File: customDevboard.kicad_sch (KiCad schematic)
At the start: 44 parts, among them J2 USB_C_Receptacle_USB2.0_14P, J20 From BEC, J6 Debug, J7 To GPS, J8 BZ+, J9 COL, Q1 BC817, Q2 AO3401A, U3 TPD2EUSB30, U5 STM32F722RET6, U6 TLV75733PDRV, Y1 8MHz, Y2 32.768KHz

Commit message: ready for production almost
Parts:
- added J1, J10, J11, J12, J13, J14, J15, J16, J17, J18, J19, J21, J22, J23, J24, J25, J26, J27, J3, J4, J5: Conn_01x01, Connector_Wire:SolderWirePad_1x01_SMD_1x2mm, symbol Connector_Generic:Conn_01x01
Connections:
- net PC3: now reaches U5.11 (PC3)
- net PC3: now also J24.1 (Pin_1)
- net PA0: now reaches U5.14 (PA0)
- net PA0: now also J25.1 (Pin_1)
- net PA1: now reaches U5.15 (PA1)
- net PA1: now also J26.1 (Pin_1)
- net PB2: now reaches U5.27 (PB2)
- net PB2: now also J27.1 (Pin_1)
- net PB12: now reaches U5.33 (PB12)
- net PB12: now also J22.1 (Pin_1)
- net PB14: now reaches U5.35 (PB14)
- net PB14: now also J21.1 (Pin_1)
- net PB15: now reaches U5.36 (PB15)
- net PB15: now also J19.1 (Pin_1)
- net PC6: now reaches U5.37 (PC6)
- net PC6: now also J18.1 (Pin_1)
- net PC7: now reaches U5.38 (PC7)
- net PC7: now also J17.1 (Pin_1)
- net PC8: now reaches U5.39 (PC8)
- net PC8: now also J16.1 (Pin_1)
- net PC9: now reaches U5.40 (PC9)
- net PC9: now also J15.1 (Pin_1)
- net PA8: now reaches U5.41 (PA8)
- net PA8: now also J14.1 (Pin_1)
- net PA15: now reaches U5.50 (PA15)
- net PA15: now also J13.1 (Pin_1)
- net PC12: now reaches U5.53 (PC12)
- net PC12: now also J12.1 (Pin_1)
- net PD2: now reaches U5.54 (PD2)
- net PD2: now also J11.1 (Pin_1)
- net PB3: now reaches U5.55 (PB3)
- net PB3: now also J10.1 (Pin_1)
- net PB4: now reaches U5.56 (PB4)
- net PB4: now also J5.1 (Pin_1)
- net PB5: now reaches U5.57 (PB5)
- net PB5: now also J4.1 (Pin_1)
- net PB8: now reaches U5.61 (PB8)
- net PB8: now also J3.1 (Pin_1)
- net PB9: now reaches U5.62 (PB9)
- net PB9: now also J1.1 (Pin_1)
- net PC0: now reaches U5.8 (PC0)
- net PC0: now also J23.1 (Pin_1)
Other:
- removed sheet ESC
- note added: "Breakout pads"
- moved on the sheet: C24, C25, C26, D1, FB1, J6, R19, TP5, Y1, Y2

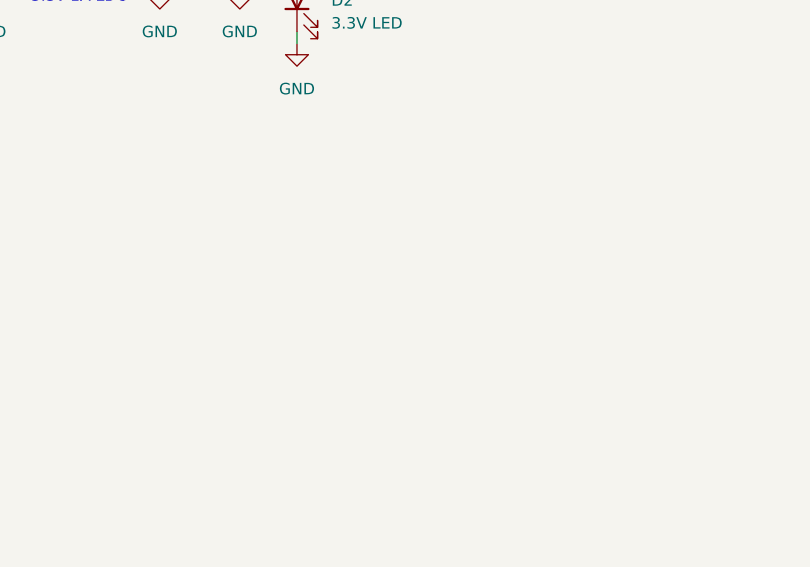
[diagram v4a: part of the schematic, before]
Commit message: fix drc issues and blender render
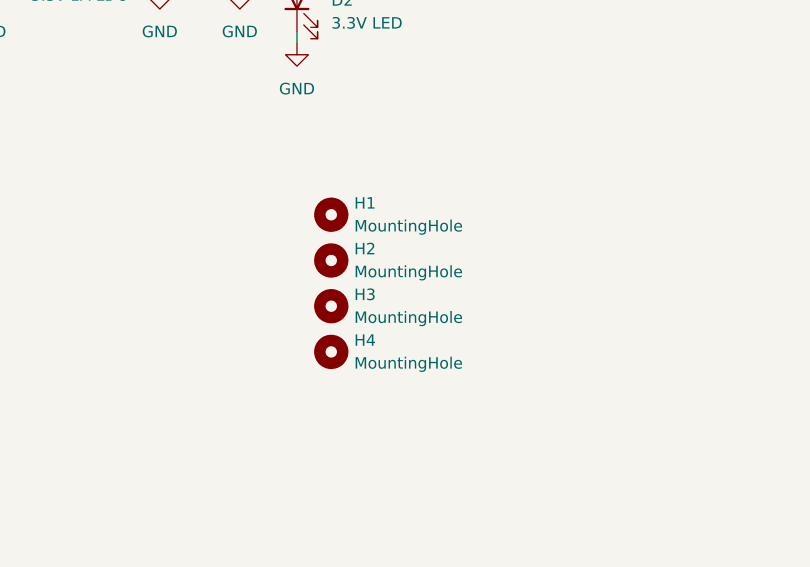
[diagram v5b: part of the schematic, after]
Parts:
- added H1, H2, H3, H4: MountingHole, MountingHole:MountingHole_3.2mm_M3, symbol Mechanical:MountingHole

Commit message: firmware and readme
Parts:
- added J28: PA6, Connector_Wire:SolderWirePad_1x01_SMD_1x2mm, symbol Connector_Generic:Conn_01x01
- added J29: PA5, Connector_Wire:SolderWirePad_1x01_SMD_1x2mm, symbol Connector_Generic:Conn_01x01
- added J30: PC1, Connector_Wire:SolderWirePad_1x01_SMD_1x2mm, symbol Connector_Generic:Conn_01x01
- added J31, J35: PC11, Connector_Wire:SolderWirePad_1x01_SMD_1x2mm, symbol Connector_Generic:Conn_01x01
- added J32: PB13, Connector_Wire:SolderWirePad_1x01_SMD_1x2mm, symbol Connector_Generic:Conn_01x01
- added J33: PA4, Connector_Wire:SolderWirePad_1x01_SMD_1x2mm, symbol Connector_Generic:Conn_01x01
- added J34: PB2, Connector_Wire:SolderWirePad_1x01_SMD_1x2mm, symbol Connector_Generic:Conn_01x01
- added J36: PC10, Connector_Wire:SolderWirePad_1x01_SMD_1x2mm, symbol Connector_Generic:Conn_01x01
- added J37: PB6, Connector_Wire:SolderWirePad_1x01_SMD_1x2mm, symbol Connector_Generic:Conn_01x01
- added J38: PB7, Connector_Wire:SolderWirePad_1x01_SMD_1x2mm, symbol Connector_Generic:Conn_01x01
- added J39: PA9, Connector_Wire:SolderWirePad_1x01_SMD_1x2mm, symbol Connector_Generic:Conn_01x01
- added J40: PA10, Connector_Wire:SolderWirePad_1x01_SMD_1x2mm, symbol Connector_Generic:Conn_01x01
- added J41: PA2, Connector_Wire:SolderWirePad_1x01_SMD_1x2mm, symbol Connector_Generic:Conn_01x01
- added J42: PA3, Connector_Wire:SolderWirePad_1x01_SMD_1x2mm, symbol Connector_Generic:Conn_01x01
- added J43: PB10, Connector_Wire:SolderWirePad_1x01_SMD_1x2mm, symbol Connector_Generic:Conn_01x01
- added J44: PB11, Connector_Wire:SolderWirePad_1x01_SMD_1x2mm, symbol Connector_Generic:Conn_01x01
- J25: value Conn_01x01 -> PA0
- J26: value Conn_01x01 -> PA1
- J27: value Conn_01x01 -> PA7
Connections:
- net I2C1_SCL: now also J37.1 (Pin_1)
- net I2C1_SDA: now also J38.1 (Pin_1)
- net SPI1_MISO: now also J28.1 (Pin_1)
- net SPI1_MOSI: now also J27.1 (Pin_1)
- net SPI1_SCK: now also J29.1 (Pin_1)
- net SPI2_MISO: now also J31.1 (Pin_1)
- net SPI2_MOSI: now also J30.1 (Pin_1)
- net SPI2_SCK: now also J32.1 (Pin_1)
- net SPI3_MISO: now also J35.1 (Pin_1)
- net SPI3_NSS: now also J33.1 (Pin_1)
- net SPI3_SCK: now also J36.1 (Pin_1)
- net USART1_RX: now also J40.1 (Pin_1)
- net USART1_TX: now also J39.1 (Pin_1)
- net USART2_RX: now also J42.1 (Pin_1)
- net USART2_TX: now also J41.1 (Pin_1)
- net USART3_RX: now also J44.1 (Pin_1)
- net USART3_TX: now also J43.1 (Pin_1)
- net PB2 renamed SPI3_MOSI
- net SPI3_MOSI: now also J34.1 (Pin_1); no longer J27.1 (Pin_1)
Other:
- note added: "For IMU"
- note added: "to GPS and barometer"
- moved on the sheet: H1, H2, H3, H4

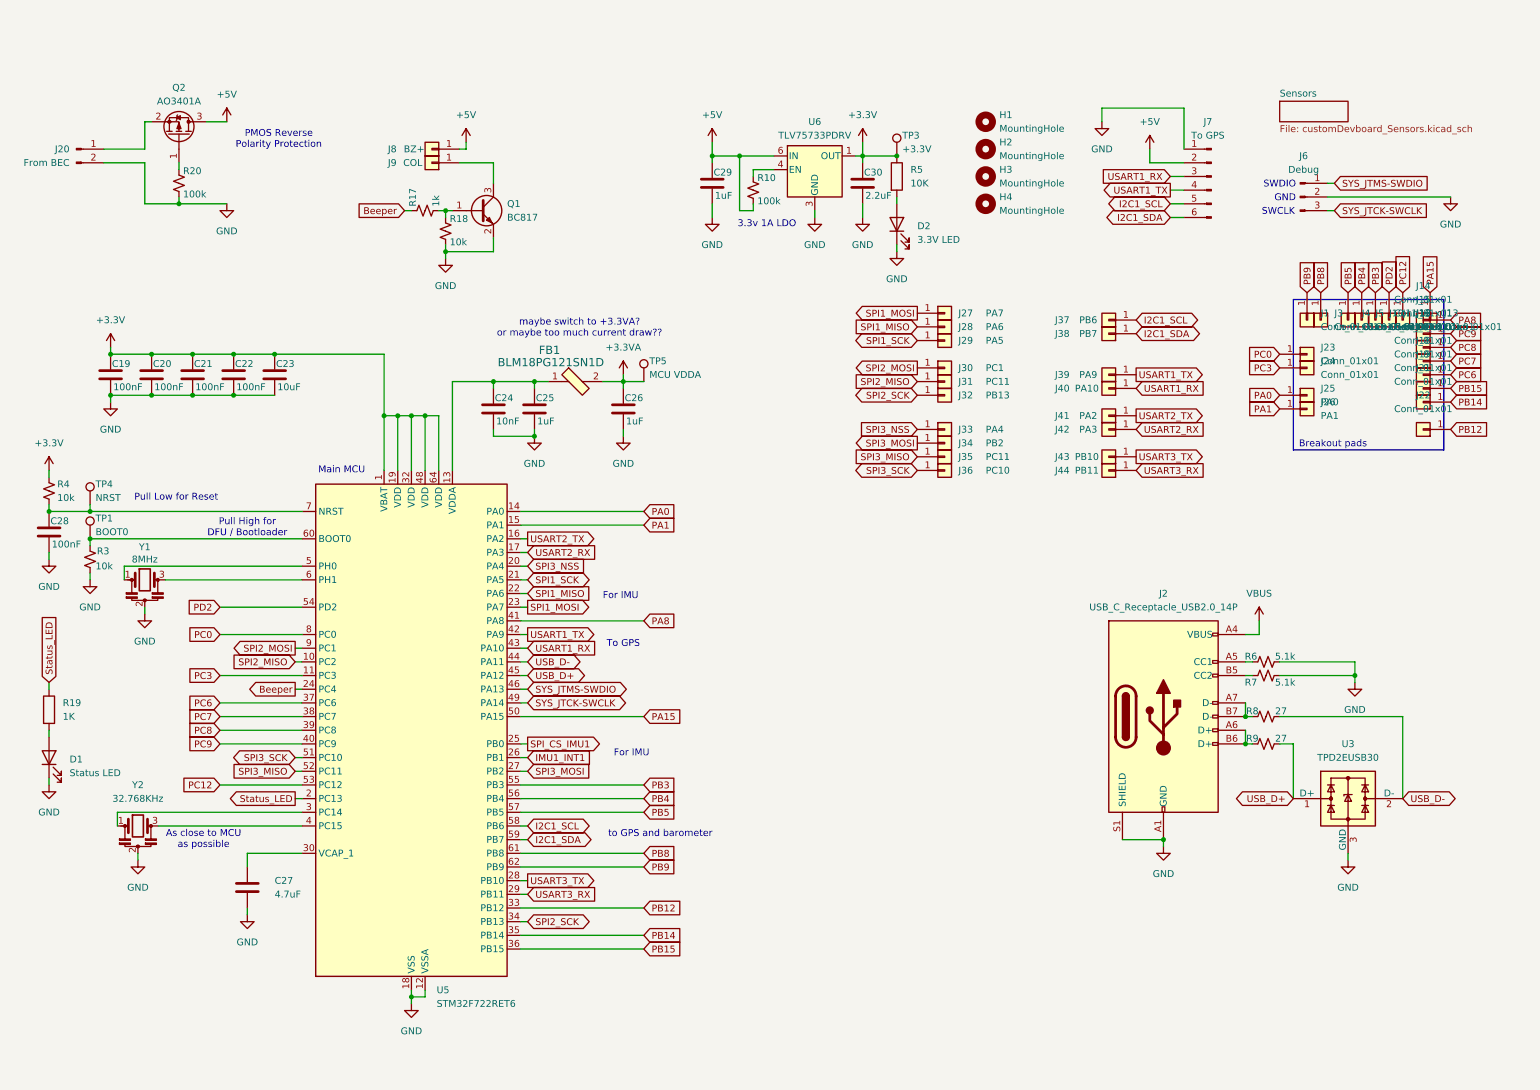
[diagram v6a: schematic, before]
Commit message: add switches and fix drc
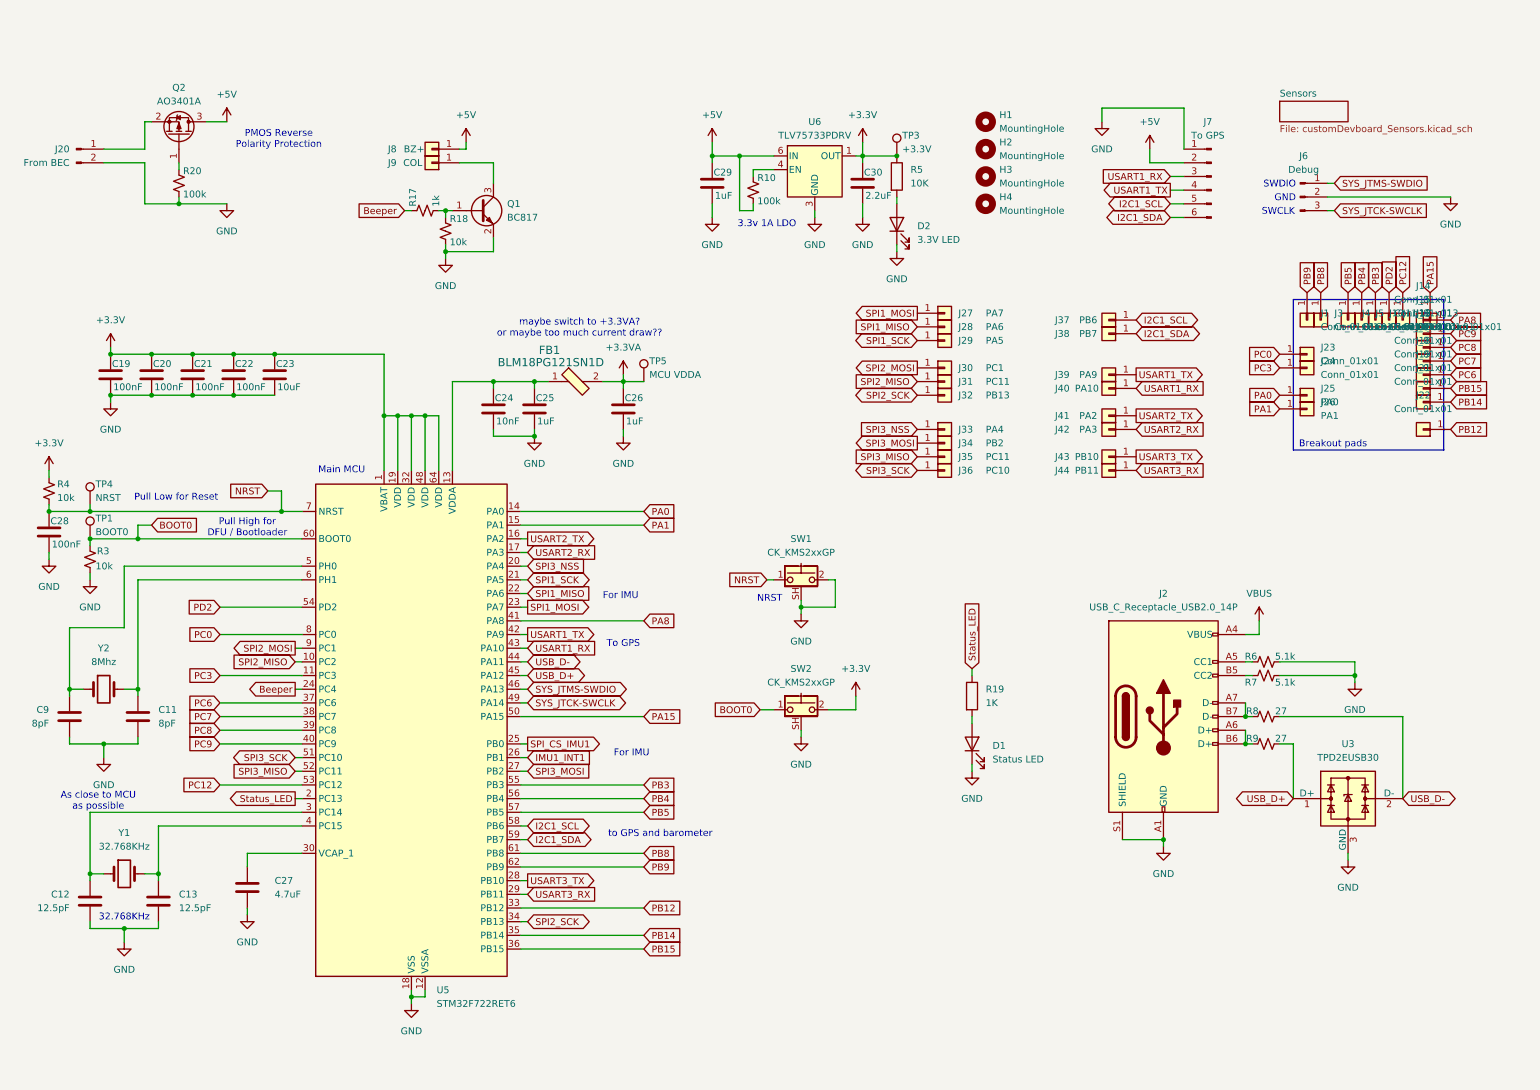
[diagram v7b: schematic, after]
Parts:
- removed Y1: 8MHz, Crystal:Resonator_SMD_Murata_CSTxExxV-3Pin_3.0x1.1mm, symbol Device:Resonator
- removed Y2: 32.768KHz, Crystal:Resonator_SMD_Murata_CSTxExxV-3Pin_3.0x1.1mm, symbol Device:Resonator
- added C11, C9: 8pF, Capacitor_SMD:C_0603_1608Metric, symbol Device:C
- added C12, C13: 12.5pF, Capacitor_SMD:C_0603_1608Metric, symbol Device:C
- added SW1, SW2: CK_KMS2xxGP, Button_Switch_SMD:SW_SPST_CK_KMS2xxGP, symbol Switch:CK_KMS2xxGP
- added Y1: 32.768KHz, Crystal:Crystal_SMD_2012-2Pin_2.0x1.2mm, symbol Device:Crystal
- added Y2: 8Mhz, Crystal:Crystal_SMD_2012-2Pin_2.0x1.2mm, symbol Device:Crystal
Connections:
- net +3.3V: now also SW2.2
- net GND: now also C11.2, C12.2, C13.2, C9.2, SW1.2, SW1.SH (B), SW2.SH (B)
- net NRST: now reaches C28.1, R4.2, TP4.1, U5.7 (NRST)
- net NRST: now also SW1.1
- net at U5.3 (PC14): now also C12.1, Y1.1
- net at U5.4 (PC15): now also C13.1, Y1.2
- net at U5.5 (PH0): now also C9.1, Y2.1
- net at U5.6 (PH1): now also C11.1, Y2.2
- net BOOT0: now reaches R3.1, TP1.1, U5.60 (BOOT0)
- net BOOT0: now also SW2.1
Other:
- note added: "32.768KHz"
- note added: "NRST"
- moved on the sheet: D1, R19

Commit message: restart pcb because too many new parts
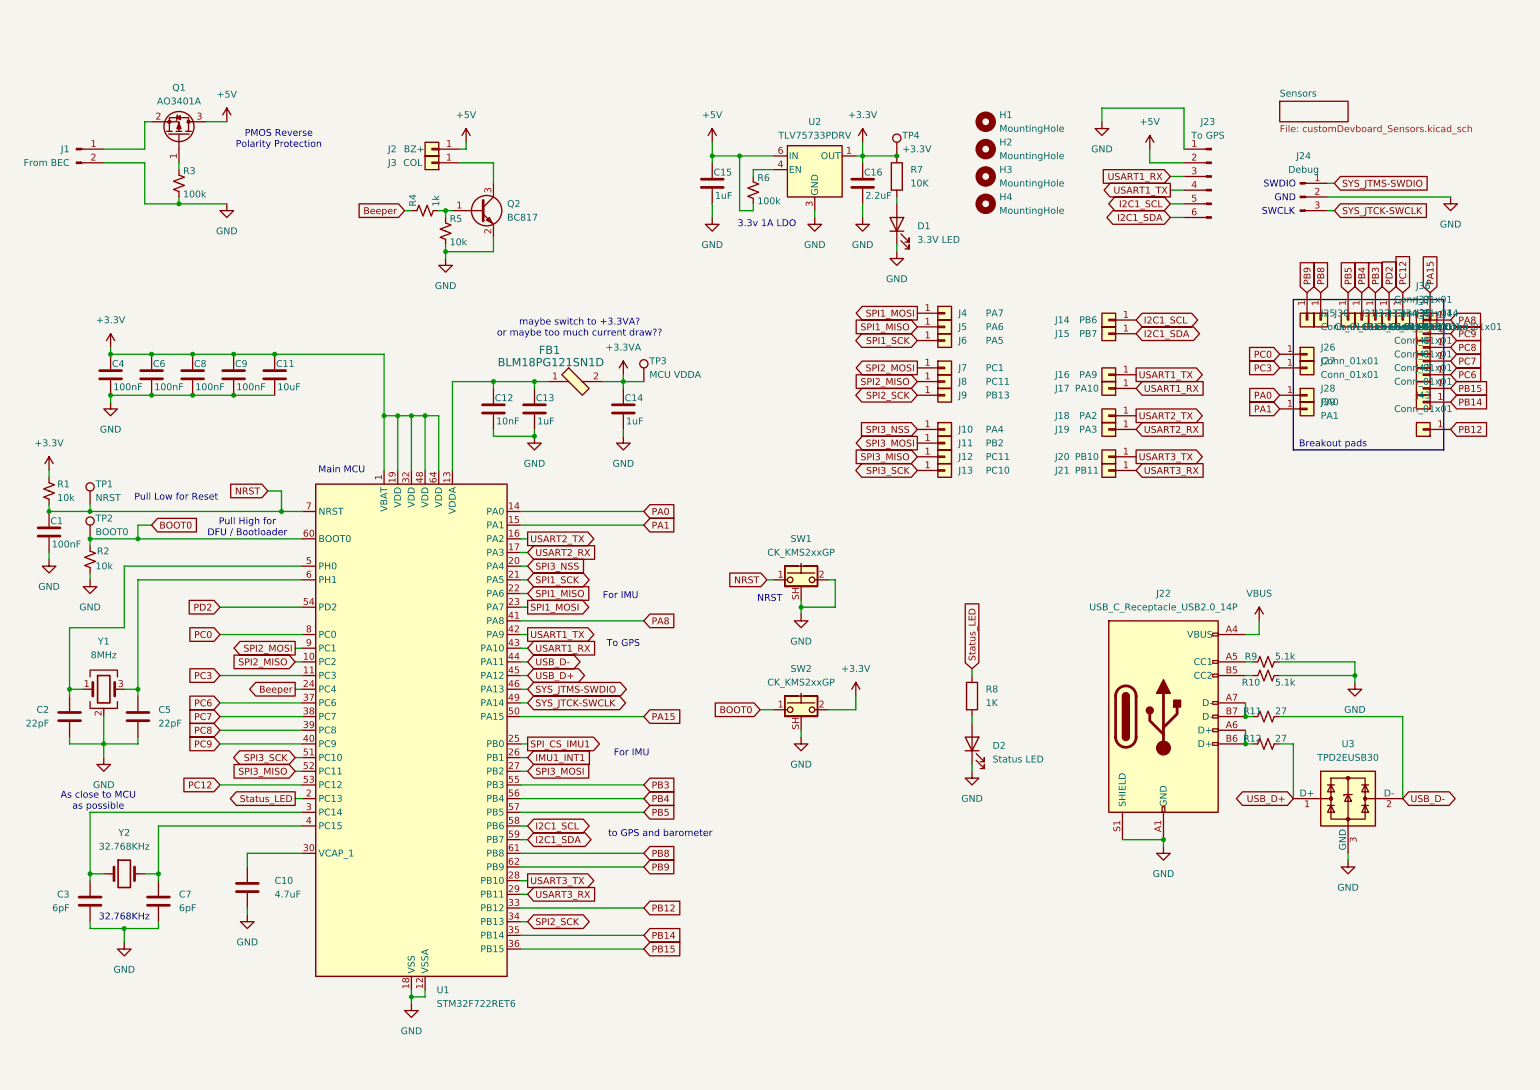
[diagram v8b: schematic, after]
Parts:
- removed Y2: 8Mhz, Crystal:Crystal_SMD_2012-2Pin_2.0x1.2mm, symbol Device:Crystal
- added Y1: 8MHz, Crystal:Crystal_SMD_3225-4Pin_3.2x2.5mm, symbol Device:Crystal_GND24
- C2: renamed from C9; value 8pF -> 22pF
- C3: renamed from C12; value 12.5pF -> 6pF
- C5: renamed from C11; value 8pF -> 22pF
- C7: renamed from C13; value 12.5pF -> 6pF
- D1: renamed from D2; footprint LED_SMD:LED_0402_1005Metric -> LED_SMD:LED_0603_1608Metric
- Y2: renamed from Y1; LCSC (none) -> C99009
- renumbered C28 to C1, C27 to C10, C23 to C11, C24 to C12, C25 to C13, C26 to C14, C29 to C15, C30 to C16, C19 to C4, C20 to C6, C21 to C8, C22 to C9, D1 to D2, J20 to J1, J33 to J10, J34 to J11, J35 to J12, J36 to J13, J37 to J14, J38 to J15, J39 to J16, J40 to J17, J41 to J18, J42 to J19, J8 to J2, J43 to J20, J44 to J21, J2 to J22, J7 to J23, J6 to J24, J1 to J25, J23 to J26, J24 to J27, J25 to J28, J26 to J29, J9 to J3, J3 to J30, J4 to J31, J5 to J32, J10 to J33, J11 to J34, J12 to J35, J14 to J36, J15 to J37, J16 to J38, J17 to J39, J27 to J4, J18 to J40, J19 to J41, J21 to J42, J22 to J43, J13 to J44, J28 to J5, J29 to J6, J30 to J7, J31 to J8, J32 to J9, Q2 to Q1, Q1 to Q2, R4 to R1, R7 to R10, R8 to R11, R9 to R12, R3 to R2, R20 to R3, R17 to R4, R18 to R5, R10 to R6, R5 to R7, R19 to R8, R6 to R9, TP4 to TP1, TP1 to TP2, TP5 to TP3, TP3 to TP4, U5 to U1, U6 to U2
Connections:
- net GND: now also Y1.2 (G), Y1.4 (G)
- net at C2.1, U1.5 (PH0): now also Y1.1
- net at C5.1, U1.6 (PH1): now also Y1.3
